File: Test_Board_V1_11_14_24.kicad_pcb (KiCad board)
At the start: 2 copper layers, 165.5 x 179.5 mm, 35 parts, among them IC1 FE1.1S, J4 Qwiic Connect

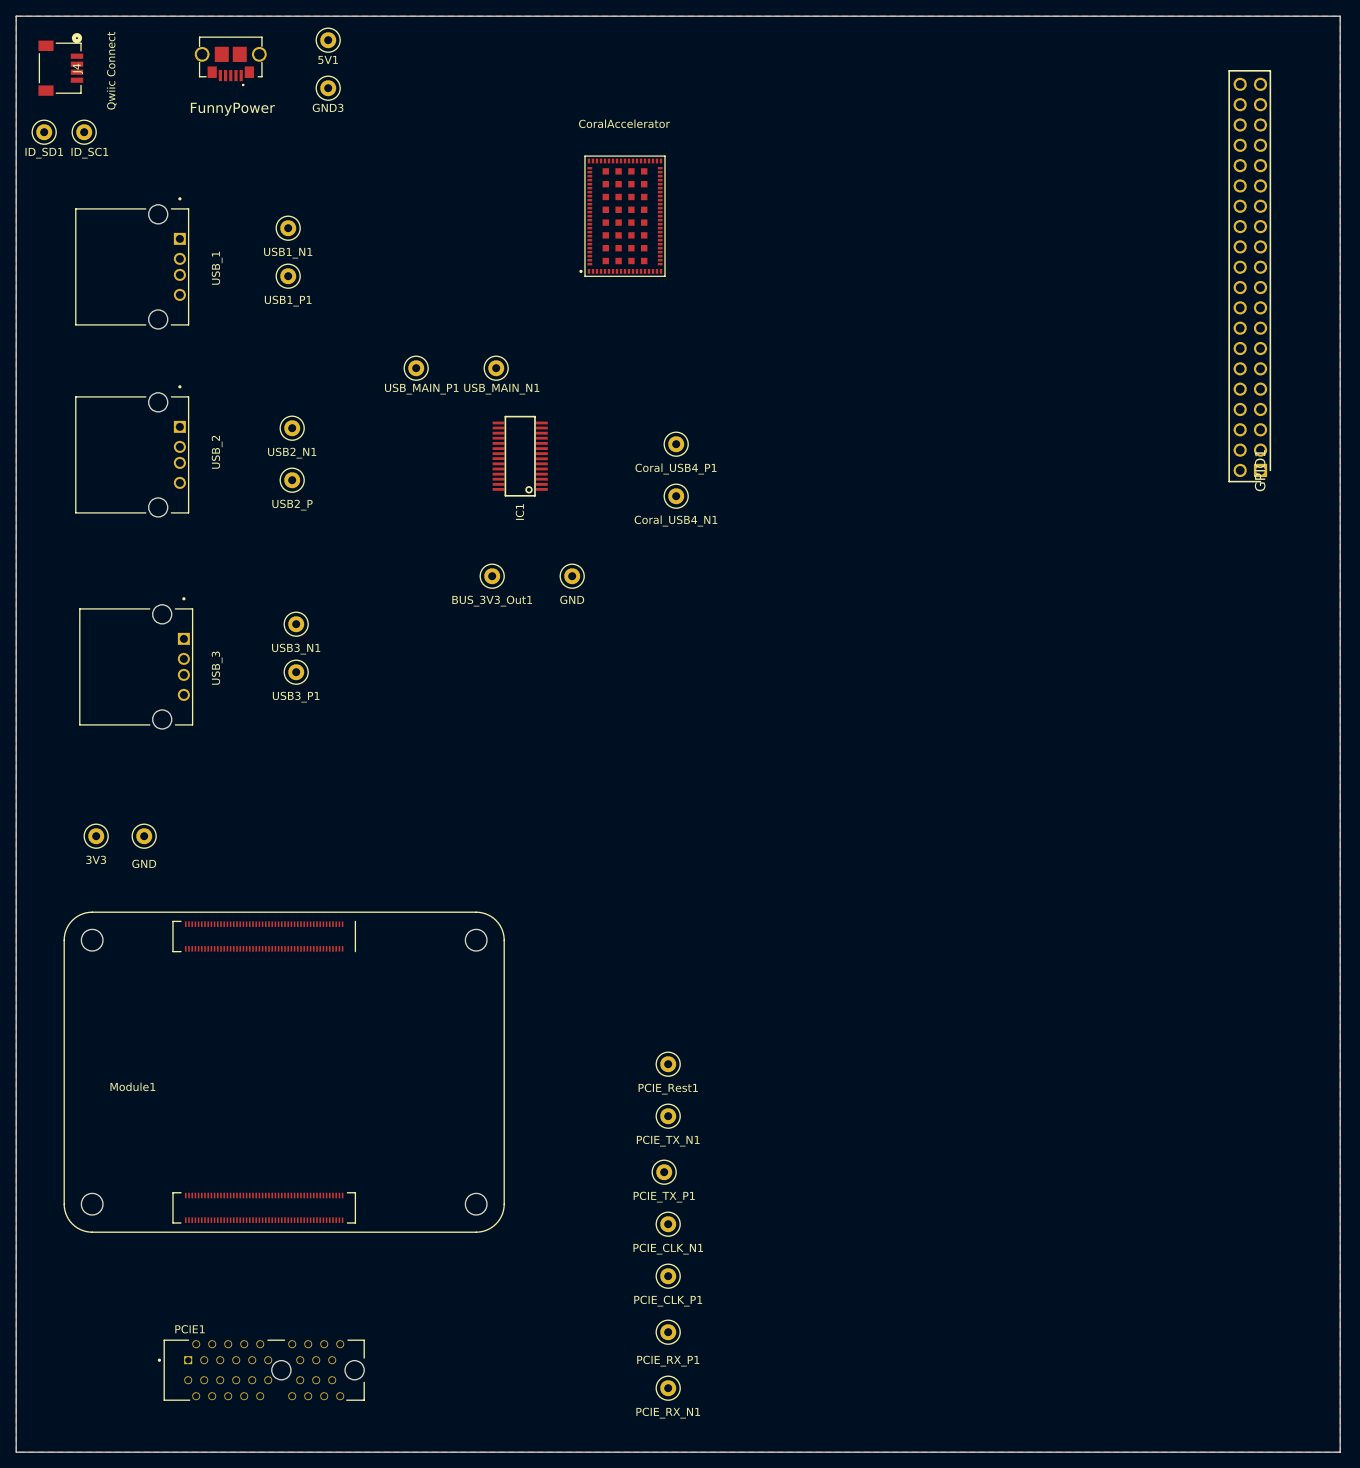
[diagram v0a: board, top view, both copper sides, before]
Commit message: All traces done except GPIO
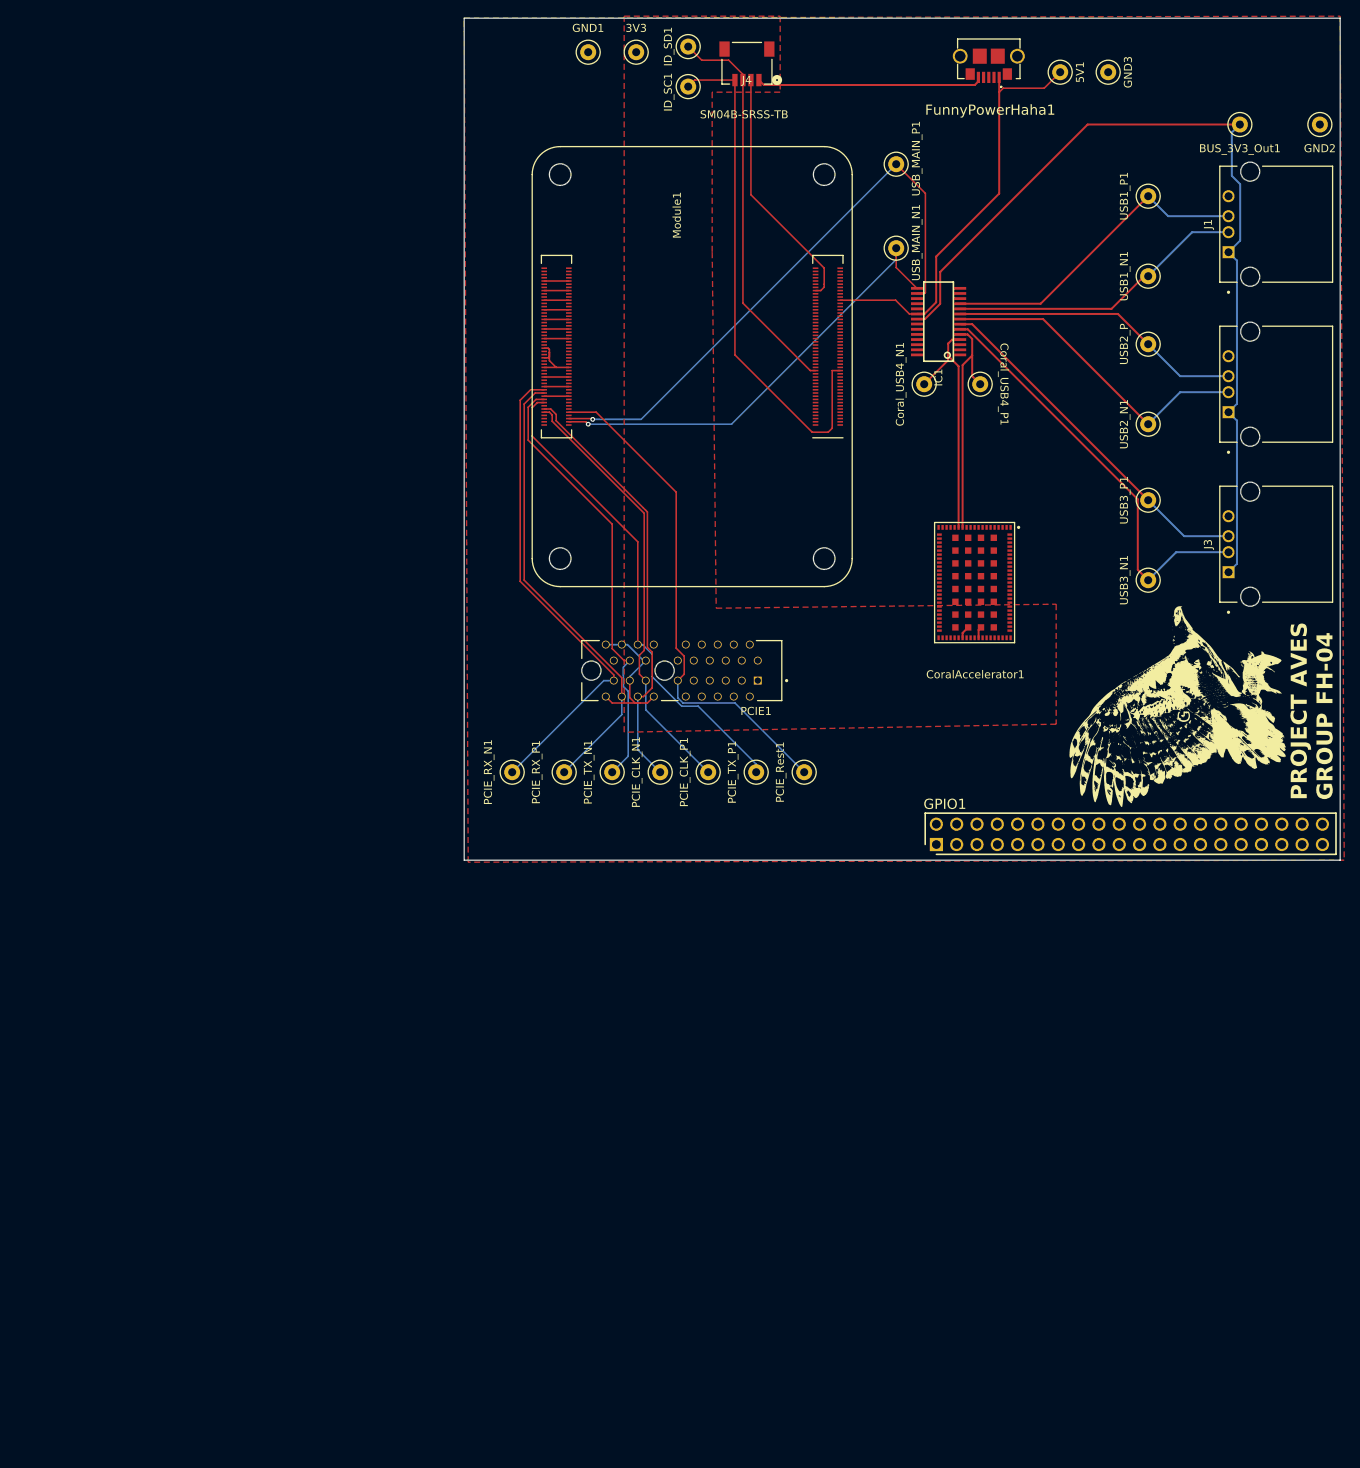
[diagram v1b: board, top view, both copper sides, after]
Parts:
- added G***: LOGO, LOGO, F.Cu at (164.5, 102.0)
- J4: value Qwiic Connect -> SM04B-SRSS-TB
- moved J3 136.9 mm to (172.8, 82.0), turned to 90 degrees
- moved J2 136.8 mm to (172.8, 62.0), turned to 90 degrees
- moved J1 136.6 mm to (172.8, 42.0), turned to 90 degrees
- moved Module1 132.4 mm to (119.5, 35.8), turned to 180 degrees
- moved 3V3 119.0 mm to (96.0, 20.5), turned to 180 degrees
- moved GND1 112.6 mm to (90.0, 20.5), turned to 180 degrees
- moved BUS_3V3_Out1 109.2 mm to (171.5, 29.5)
- moved GND2 109.2 mm to (181.5, 29.5)
- moved USB3_P1 108.6 mm to (160.0, 76.5), turned to -90 degrees
- moved USB2_P1 108.3 mm to (160.0, 57.0), turned to -90 degrees
- moved USB1_P1 108.0 mm to (160.0, 38.5), turned to -90 degrees
- moved USB1_N1 107.7 mm to (160.0, 48.5), turned to -90 degrees
- moved USB2_N1 107.0 mm to (160.0, 67.0), turned to -90 degrees
- moved USB3_N1 106.6 mm to (160.0, 86.5), turned to -90 degrees
- moved PCIE1 101.8 mm to (101.7, 97.8), turned to 180 degrees
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- renumbered CoralAccelerator to CoralAccelerator1, FunnyPower to FunnyPowerHaha1, GND to GND1, GND to GND2, USB_1 to J1, USB_2 to J2, USB_3 to J3
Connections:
- GPIO1 pad 10: GPIO_10 -> unconnected-(GPIO1-Pad10)
- GPIO1 pad 11: GPIO_11 -> unconnected-(GPIO1-Pad11)
- GPIO1 pad 12: GPIO_12 -> unconnected-(GPIO1-Pad12)
- GPIO1 pad 13: GPIO_13 -> unconnected-(GPIO1-Pad13)
- GPIO1 pad 14: GPIO_14 -> unconnected-(GPIO1-Pad14)
- GPIO1 pad 15: GPIO_15 -> unconnected-(GPIO1-Pad15)
- GPIO1 pad 16: GPIO_16 -> unconnected-(GPIO1-Pad16)
- GPIO1 pad 17: GPIO_17 -> unconnected-(GPIO1-Pad17)
- GPIO1 pad 18: GPIO_18 -> unconnected-(GPIO1-Pad18)
- GPIO1 pad 19: GPIO_19 -> unconnected-(GPIO1-Pad19)
- GPIO1 pad 2: GPIO_2 -> unconnected-(GPIO1-Pad2)
- GPIO1 pad 20: GPIO_20 -> unconnected-(GPIO1-Pad20)
- GPIO1 pad 21: GPIO_21 -> unconnected-(GPIO1-Pad21)
- GPIO1 pad 22: GPIO_22 -> unconnected-(GPIO1-Pad22)
- GPIO1 pad 23: GPIO_23 -> unconnected-(GPIO1-Pad23)
- GPIO1 pad 24: GPIO_24 -> unconnected-(GPIO1-Pad24)
- GPIO1 pad 25: GPIO_25 -> unconnected-(GPIO1-Pad25)
- GPIO1 pad 26: GPIO_26 -> unconnected-(GPIO1-Pad26)
- GPIO1 pad 27: GPIO_27 -> unconnected-(GPIO1-Pad27)
- GPIO1 pad 3: GPIO_3 -> unconnected-(GPIO1-Pad3)
- GPIO1 pad 38: +3V3 -> unconnected-(GPIO1-Pad38)
- GPIO1 pad 4: GPIO_4 -> unconnected-(GPIO1-Pad4)
- GPIO1 pad 40: +5V -> unconnected-(GPIO1-Pad40)
- GPIO1 pad 5: GPIO_5 -> unconnected-(GPIO1-Pad5)
- GPIO1 pad 6: GPIO_6 -> unconnected-(GPIO1-Pad6)
- GPIO1 pad 7: GPIO_7 -> unconnected-(GPIO1-Pad7)
- GPIO1 pad 8: GPIO_8 -> unconnected-(GPIO1-Pad8)
- GPIO1 pad 9: GPIO_9 -> unconnected-(GPIO1-Pad9)
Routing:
- net BUS_3v3_Out: track 0.00 -> 112.0 mm
- net GND: track 0.00 -> 89.9 mm
- net USB_MAIN_P: track 0.00 -> 72.8 mm, vias 0 -> 1
- net ID_SC: track 0.00 -> 65.1 mm
- net PCIE_Reset: track 0.00 -> 63.7 mm
- net PCIE_Connector_RX_N: track 0.00 -> 60.9 mm
- net PCIE_Connector_TX_P: track 0.00 -> 60.5 mm
- net PCIE_Connector_RX_P: track 0.00 -> 57.1 mm
- net USB_MAIN_N: track 0.00 -> 57.1 mm, vias 0 -> 1
- net PCIE_Connector_TX_N: track 0.00 -> 55.1 mm
- net PCIE_CLK_P: track 0.00 -> 54.4 mm
- net PCIE_CLK_N: track 0.00 -> 54.1 mm
- net +5V: track 0.00 -> 53.3 mm
- net USB_SUB3_N: track 0.00 -> 53.1 mm
- net ID_SD: track 0.00 -> 49.4 mm
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- added copper zone on F.Cu, net +3V3
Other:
- board size 165.5 x 179.5 mm -> 109.5 x 105.2 mm
- board text added: "Coral_USB4_P1"
- board text added: "PROJECT AVES GROUP FH-04"

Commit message: more traces done
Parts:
- moved Coral_USB4_N1 10.4 mm to (140.5, 68.0)
- moved Coral_USB4_P1 1.80 mm to (140.5, 63.0)
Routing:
- net GND: track 89.9 -> 180.8 mm
- net BUS_3v3_Out: track 112.0 -> 125.5 mm
- net +3V3: track 30.9 -> 40.3 mm
- net USB_SUB4_N: track 30.0 -> 28.6 mm

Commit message: pcie connector fixed
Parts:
- PCIE1: footprint SeniorDesign_PCIEConnector:AMPHENOL_10082378-11100TLF -> 10018783-11110TLF:AMPHENOL_10018783-11110TLF
- moved USB1_N1 10.0 mm to (160.0, 38.5)
- moved USB1_P1 10.0 mm to (160.0, 48.5)
- moved USB2_N1 10.0 mm to (160.0, 57.0)
- moved USB2_P1 10.0 mm to (160.0, 67.0)
- moved USB3_N1 10.0 mm to (160.0, 76.5)
- moved USB3_P1 10.0 mm to (160.0, 86.5)
- moved PCIE1 8.57 mm to (93.8, 101.2)
- moved PCIE_CLK_P1 6.00 mm to (111.0, 110.5)
- moved PCIE_TX_P1 6.00 mm to (105.0, 110.5)
- moved Coral_USB4_N1 5.00 mm to (140.5, 63.0)
- moved Coral_USB4_P1 5.00 mm to (140.5, 68.0)
- renumbered BUS_3V3_Out1 to 3V3_Out1
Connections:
- GPIO1 pad 38: unconnected-(GPIO1-Pad38) -> +3V3
- GPIO1 pad 40: unconnected-(GPIO1-Pad40) -> +5V
- IC1 pad 1: GND -> unconnected-(IC1-VSS-Pad1)
- IC1 pad 10: USB_SUB1_N -> USB_SUB1_P
- IC1 pad 11: USB_SUB1_P -> USB_SUB1_N
- IC1 pad 4: USB_SUB4_N -> USB_SUB4_P
- IC1 pad 5: USB_SUB4_P -> USB_SUB4_N
- IC1 pad 6: USB_SUB3_N -> USB_SUB3_P
- IC1 pad 7: USB_SUB3_P -> USB_SUB3_N
- IC1 pad 8: USB_SUB2_N -> USB_SUB2_P
- IC1 pad 9: USB_SUB2_P -> USB_SUB2_N
- J1 pad 1: BUS_3v3_Out -> +5V
- J2 pad 1: BUS_3v3_Out -> +5V
- J3 pad 1: BUS_3v3_Out -> +5V
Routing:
- net +5V: track 53.3 -> 188.7 mm
- net BUS_3v3_Out: track 125.5 -> 52.8 mm
- net +3V3: track 40.3 -> 103.4 mm
- net GND: track 180.8 -> 162.2 mm
- net USB_SUB3_P: track 44.5 -> 56.4 mm
- net PCIE_CLK_P: track 54.4 -> 65.2 mm
- net USB_SUB2_P: track 36.8 -> 41.5 mm
- net PCIE_Reset: track 63.7 -> 68.1 mm
- net USB_SUB1_N: track 37.5 -> 41.0 mm
- net USB_SUB3_N: track 53.1 -> 49.7 mm
- net USB_SUB2_N: track 40.6 -> 37.6 mm
- net PCIE_CLK_N: track 54.1 -> 56.8 mm
- net PCIE_Connector_RX_P: track 57.1 -> 54.7 mm
- net USB_SUB1_P: track 40.1 -> 38.3 mm
- net PCIE_Connector_RX_N: track 60.9 -> 59.2 mm
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- added copper zone on B.Cu, net GND
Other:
- board size 109.5 x 105.2 mm -> 109 x 105.2 mm
